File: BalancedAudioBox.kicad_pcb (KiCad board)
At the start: 2 copper layers, 81 x 73 mm, 66 parts, among them IC1 TPS61252DSGT, IC2 DRV135UA_2K5, IC3 DRV135UA_2K5, J1 Conn_02x10_Odd_Even, J2 Conn_01x02, J3 XLR3_Ground, J4 XLR3_Ground, J5 Conn_01x03, J6 Conn_01x02, J7 Conn_01x06, J8 Conn_01x03, U1 LM27762, U2 PCM5102, U3 AP1117-33

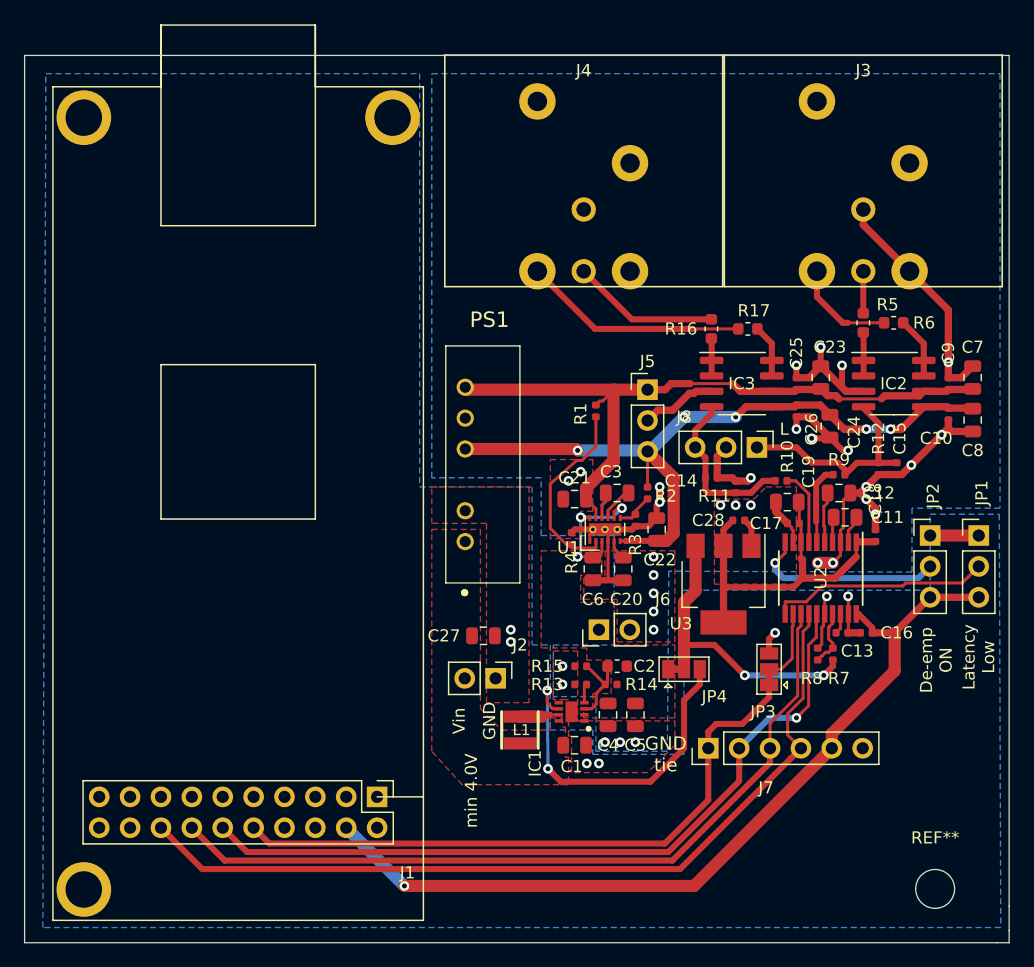
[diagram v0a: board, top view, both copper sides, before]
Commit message: smaller package, drc
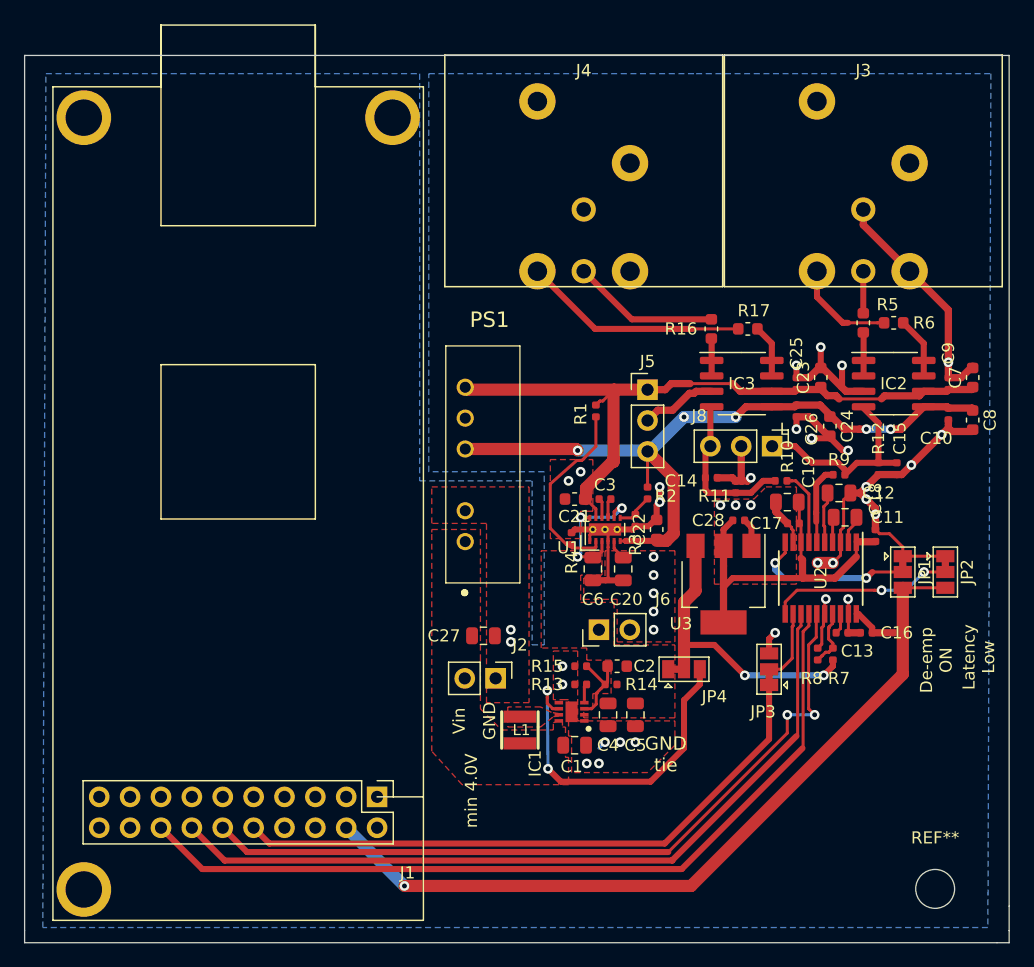
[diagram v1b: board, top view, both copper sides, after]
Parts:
- removed J7: Conn_01x06, Connector_PinHeader_2.54mm:PinHeader_1x06_P2.54mm_Vertical
- C21, C22, C23, C24, C7, C8: footprint Capacitor_SMD:C_0805_2012Metric -> Capacitor_SMD:C_0603_1608Metric
- C3: value 4.7u -> 1u; footprint Capacitor_SMD:C_0805_2012Metric -> Capacitor_SMD:C_0402_1005Metric
- JP1: value Latency -> De-emphasis; footprint Connector_PinHeader_2.54mm:PinHeader_1x03_P2.54mm_Vertical -> Jumper:SolderJumper-3_P1.3mm_Bridged12_Pad1.0x1.5mm
- JP2: value De-emphasis -> Latency; footprint Connector_PinHeader_2.54mm:PinHeader_1x03_P2.54mm_Vertical -> Jumper:SolderJumper-3_P1.3mm_Bridged12_Pad1.0x1.5mm
- JP4: value SolderJumper_3_Bridged12 -> Power source
- moved JP1 6.93 mm to (182.2, 105.5), turned to 270 degrees
- moved JP2 3.25 mm to (185.8, 105.5), turned to 270 degrees
- moved J8 1.25 mm to (171.5, 95.2)
- moved C3 1.12 mm to (157.8, 99.5)
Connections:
- net /PowerSupply/SW renamed /PowerSupply/SWITCH
- JP1 pad 2: /DAC/LATENCY -> /DAC/DEEMP
- JP2 pad 2: /DAC/DEEMP -> /DAC/LATENCY
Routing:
- net +3V3: track 70.4 -> 73.6 mm
- net /PowerSupply/SWITCH: track 3.05 -> 0.00 mm
- net /DAC/LATENCY: track 18.1 -> 15.2 mm, vias 0 -> 2
- net GND: track 118.4 -> 121.1 mm
- net /DAC/DEEMP: track 16.0 -> 13.6 mm, vias 1 -> 2
- net Net-(C3-Pad2): track 3.31 -> 1.95 mm
- net /MCLK: track 52.2 -> 51.0 mm
- net /DAC/LEFT: track 18.1 -> 16.9 mm
- net /DIN: track 70.4 -> 69.6 mm
- net /DAC/RIGHT: track 14.0 -> 13.3 mm
- net Net-(C3-Pad1): track 2.18 -> 1.65 mm
- net /LRCLK: track 63.4 -> 63.9 mm, vias 1 -> 2
- added copper zone on F.Cu, net /PowerSupply/SWITCH

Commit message: final tweaks
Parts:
- moved L1 0.75 mm to (151.5, 118.5)
- moved R9 0.71 mm to (176.5, 97.0), turned to 270 degrees
- moved C23 0.25 mm to (175.5, 89.8)
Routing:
- net GND: track 121.1 -> 48.0 mm, vias 39 -> 68
- net +5.4V: track 12.1 -> 14.4 mm
- net VIN: track 28.4 -> 26.8 mm, vias 2 -> 0
- net /DAC/LEFT: track 16.9 -> 15.8 mm
- net -5V: track 60.6 -> 61.3 mm
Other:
- board text removed: "GND tie"
- board text removed: "L"
